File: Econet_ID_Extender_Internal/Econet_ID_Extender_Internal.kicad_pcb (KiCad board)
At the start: 2 copper layers, 34.5 x 14 mm, 3 parts, among them J1 Conn_01x03_Male, J2 Conn_02x08_Odd_Even, J3 Conn_02x06_Odd_Even

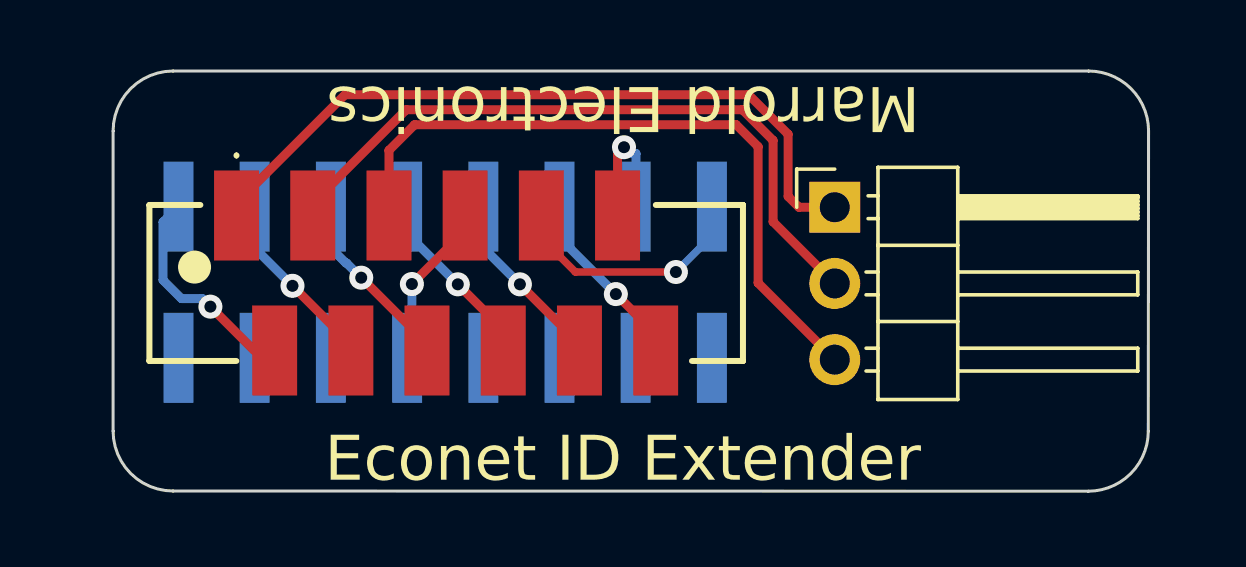
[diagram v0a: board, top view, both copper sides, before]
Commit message: Swap to standard 2.54 pitch ribbon
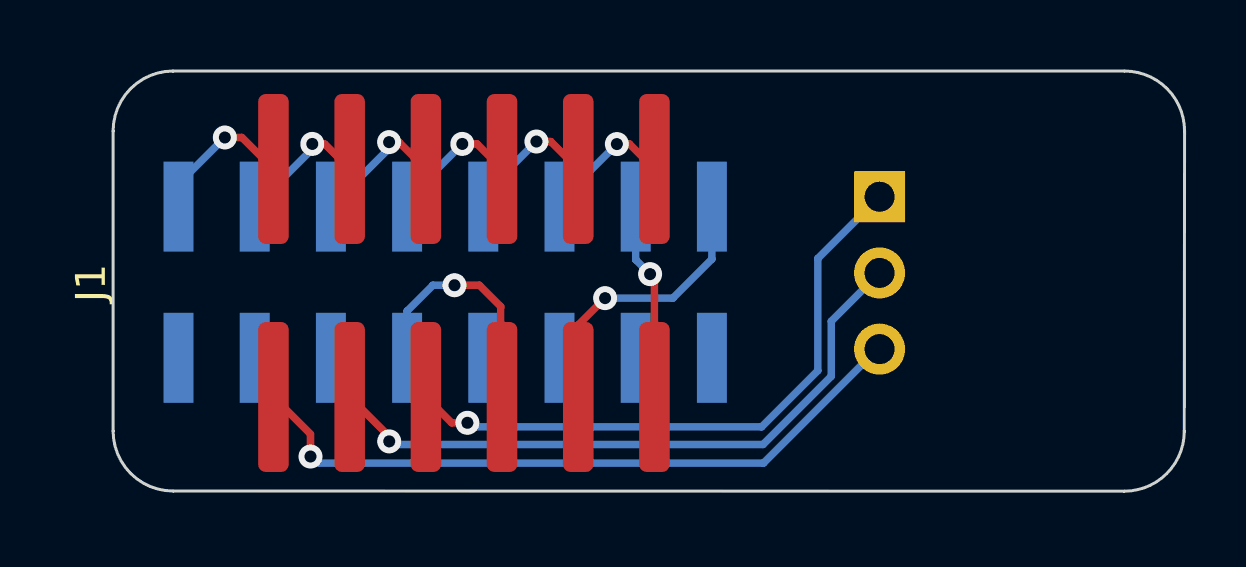
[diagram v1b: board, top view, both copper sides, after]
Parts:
- J1: value Conn_01x03_Male -> Conn_02x06_Odd_Even; footprint Connector_PinHeader_2.54mm:PinHeader_1x03_P2.54mm_Horizontal -> Connector_IDC:IDC-Header_2x06_P2.54mm_Vertical_SMD
- J3: value Conn_02x06_Odd_Even -> Conn_01x03_Male; footprint AliExpress_Stuff:MicroMatch-12p-SMD -> Connector_PinHeader_2.54mm:PinHeader_1x03_P2.54mm_Horizontal
- moved J3 14.7 mm to (158.1, 89.7)
- moved J1 12.6 mm to (144.2, 92.6), turned to 90 degrees
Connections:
- J1 pad 2: /I_AUD2 -> /I_SID_0
- J1 pad 3: /I_AUD1 -> /I_AUD2
- J3 pad 1: /I_AUD3 -> /I_AUD1
- J3 pad 2: /I_SID_0 -> /I_AUD2
- J3 pad 3: /I_AUD2 -> /I_AUD3
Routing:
- net /I_GND: track 5.55 -> 8.36 mm
- net /I_AUD1: track 23.3 -> 20.9 mm, vias 0 -> 1
- net /I_SID_0: track 7.35 -> 5.00 mm
- net /I_SID_6: track 4.63 -> 6.60 mm
- net /I_SID_5: track 6.12 -> 4.47 mm
- net /I_SID_1: track 6.12 -> 4.48 mm
- net /I_SID_3: track 6.12 -> 4.52 mm
- net /I_SID_2: track 6.14 -> 4.55 mm
- net /I_AUD3: track 24.6 -> 23.1 mm, vias 0 -> 1
- net /I_SID_4: track 6.12 -> 4.68 mm
- net /I_AUD2: track 23.1 -> 21.9 mm, vias 0 -> 1
- net /I_SID_7: track 8.38 -> 9.51 mm
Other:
- board size 34.5 x 14 mm -> 35.7 x 14 mm
- board text removed: "Econet ID Extender"
- board text removed: "Marrold Electronics"
